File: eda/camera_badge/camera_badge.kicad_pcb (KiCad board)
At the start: 2 copper layers, 111.7 x 76.2 mm, 2 parts, among them U1 ESP32-WROOM-32-DEVKIT

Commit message: badge eda updates
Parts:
- added G***: Silk01, 0_badge:camera_badge_silk01, F.Cu at (97.3, 123.4)
- added G***: Edge, 0_badge:camera_badge_edgecuts, F.Cu at (97.2, 123.3)
- DS1: footprint 0_local:GC9A01_TFT -> 0_local:GC9A01_TFT_Back_Mount
- U1: footprint 0_local:ESP32_DEVKIT_V1 -> 0_local:ESP32_DEVKIT_V1_Back_Mount
- moved U1 96.1 mm to (61.7, 165.2)
- moved DS1 78.5 mm to (84.7, 155.6)
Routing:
- net D23: track 41.0 -> 0.00 mm
- net D18: track 39.6 -> 0.00 mm
- net D16: track 32.6 -> 0.00 mm
- net D4: track 22.1 -> 0.00 mm
- net D5: track 22.0 -> 0.00 mm
- net +3.3V: track 19.9 -> 0.00 mm
- net GND: track 19.9 -> 0.00 mm
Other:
- board size 111.7 x 76.2 mm -> 115 x 204.7 mm

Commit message: eda update
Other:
- board text added: "-- Inside --"
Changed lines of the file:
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@@
     (property "ki_keywords" "GC9A01 TFT Display")
     (attr through_hole)
-    (fp_text reference "DS1" (at -1.5 -2.7) (layer "B.SilkS")
+    (fp_text reference "DS1" (at -1.96 -5.33 180 unlocked) (layer "B.SilkS")
         (effects (font (size 1 1) (thickness 0.15)) (justify mirror))
     )
     (fp_text value "GC9A01 TFT Display" (at 23.25 15.55) (layer "B.Fab")
-        (effects (font (size 1 1) (thickness 0.15)) (justify mirror))
+        (effects (font (size 1 1) (thickness 0.15)))
     )
-    (fp_text user "SCL" (at -2.3 5.15) (layer "B.SilkS")
+    (fp_text user "SCL" (at -2.3 5.15 180 unlocked) (layer "B.SilkS")
         (effects (font (size 0.75 0.75) (thickness 0.15)) (justify mirror))
     )
-    (fp_text user "GND" (at -2.3 2.65) (layer "B.SilkS")
+    (fp_text user "GND" (at -2.3 2.65 180 unlocked) (layer "B.SilkS")
         (effects (font (size 0.75 0.75) (thickness 0.15)) (justify mirror))
     )
-    (fp_text user "CS" (at -2.3 12.78) (layer "B.SilkS")
+    (fp_text user "CS" (at -2.3 12.78 180 unlocked) (layer "B.SilkS")
         (effects (font (size 0.75 0.75) (thickness 0.15)) (justify mirror))
     )
-    (fp_text user "DC" (at -2.3 10.18) (layer "B.SilkS")
+    (fp_text user "DC" (at -2.3 10.18 180 unlocked) (layer "B.SilkS")
         (effects (font (size 0.75 0.75) (thickness 0.15)) (justify mirror))
     )
-    (fp_text user "SDA" (at -2.3 7.72) (layer "B.SilkS")
+    (fp_text user "SDA" (at -2.3 7.72 180 unlocked) (layer "B.SilkS")
         (effects (font (size 0.75 0.75) (thickness 0.15)) (justify mirror))
     )
-    (fp_text user "RST" (at -2.3 15.15) (layer "B.SilkS")
+    (fp_text user "RST" (at -2.3 15.15 180 unlocked) (layer "B.SilkS")
         (effects (font (size 0.75 0.75) (thickness 0.15)) (justify mirror))
     )
-    (fp_text user "VCC" (at -2.3 0.11) (layer "B.SilkS")
+    (fp_text user "VCC" (at -2.3 0.11 180 unlocked) (layer "B.SilkS")
         (effects (font (size 0.75 0.75) (thickness 0.15)) (justify mirror))
     )
@@
     (property "ki_keywords" "RF Radio BT ESP ESP32 Espressif onboard PCB antenna")
     (attr through_hole)
-    (fp_text reference "U1" (at -11.355 -27.36) (layer "B.SilkS")
+    (fp_text reference "U1" (at -11.355 -27.36 180 unlocked) (layer "B.SilkS")
         (effects (font (size 1 1) (thickness 0.15)) (justify mirror))
     )
     (fp_text value "ESP32-WROOM-32-DEVKIT" (at -0.56 27.36) (layer "B.Fab")
-        (effects (font (size 1 1) (thickness 0.15)) (justify mirror))
+        (effects (font (size 1 1) (thickness 0.15)))
     )
-    (fp_text user "ESP32 DEVKIT" (at 0 -15.75 unlocked) (layer "B.SilkS")
+    (fp_text user "ESP32 DEVKIT" (at 0 -15.75 180 unlocked) (layer "B.SilkS")
         (effects (font (size 1 1) (thickness 0.15)) (justify mirror))
     )
-    (fp_text user "USB" (at 0 -22 unlocked) (layer "B.SilkS")
+    (fp_text user "USB" (at 0 -22 180 unlocked) (layer "B.SilkS")
         (effects (font (size 0.75 0.75) (thickness 0.1)) (justify mirror))
     )
@@
     (pad "" np_thru_hole circle (at 23.65 1.25) (size 0.5 0.5) (drill 0.5) (layers "*.Cu" "*.Mask"))
   )
+  (gr_text "-- Inside --" (at 113.8 122) (layer "B.SilkS")
+    (effects (font (size 1 1) (thickness 0.15)) (justify left bottom mirror))
+  )
+  (gr_text "-- Inside --" (at 102.7 125.9 180) (layer "B.SilkS")
+    (effects (font (size 1 1) (thickness 0.15)) (justify left bottom mirror))
+  )
 )

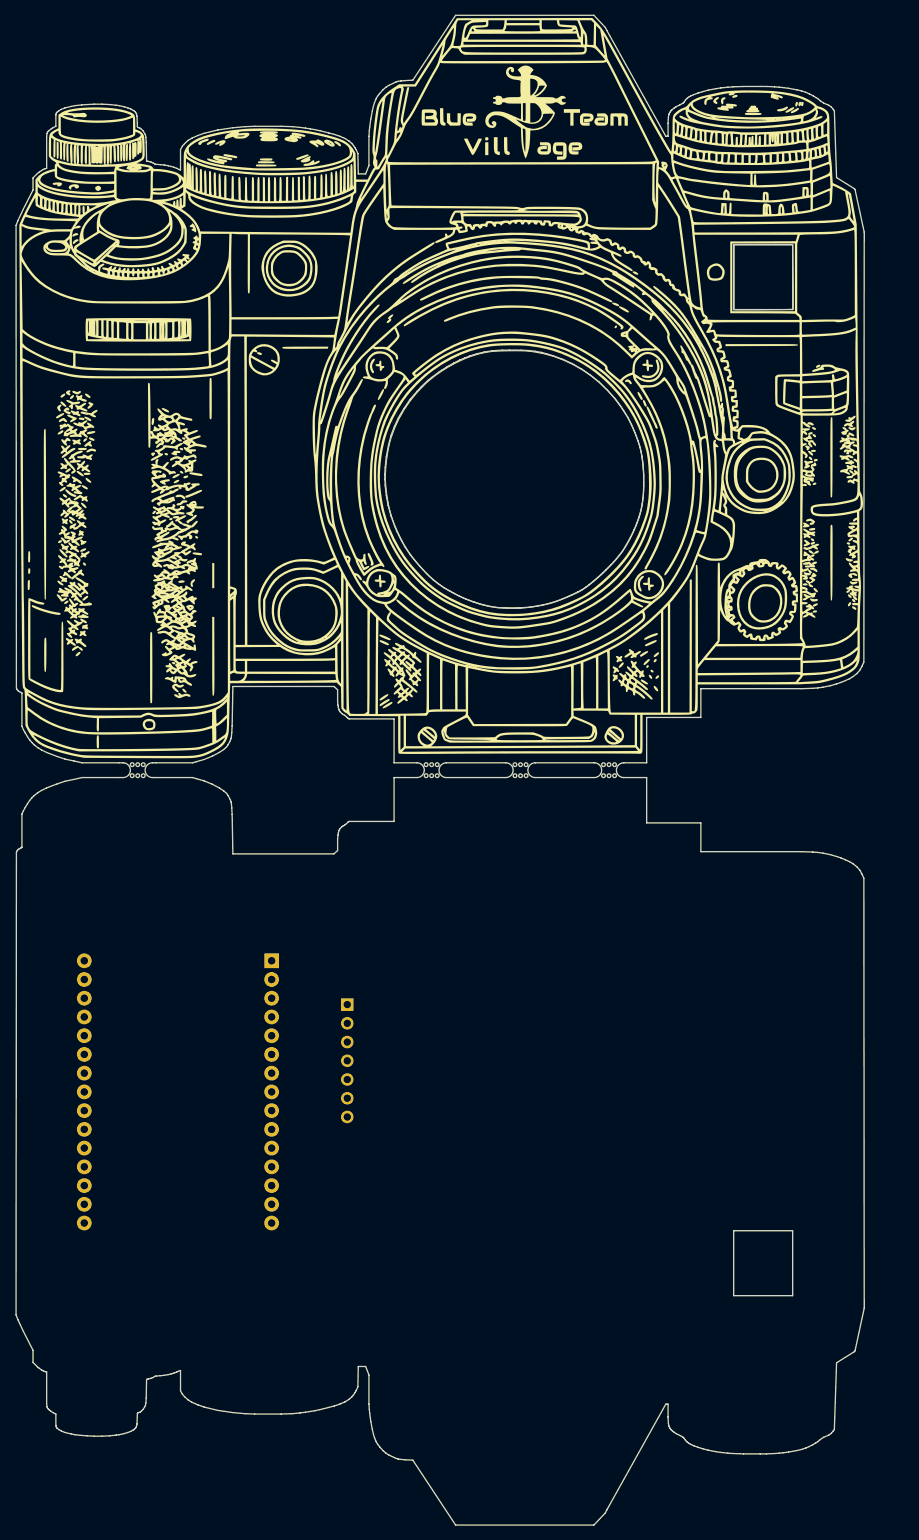
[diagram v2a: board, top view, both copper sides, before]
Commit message: made badge wider
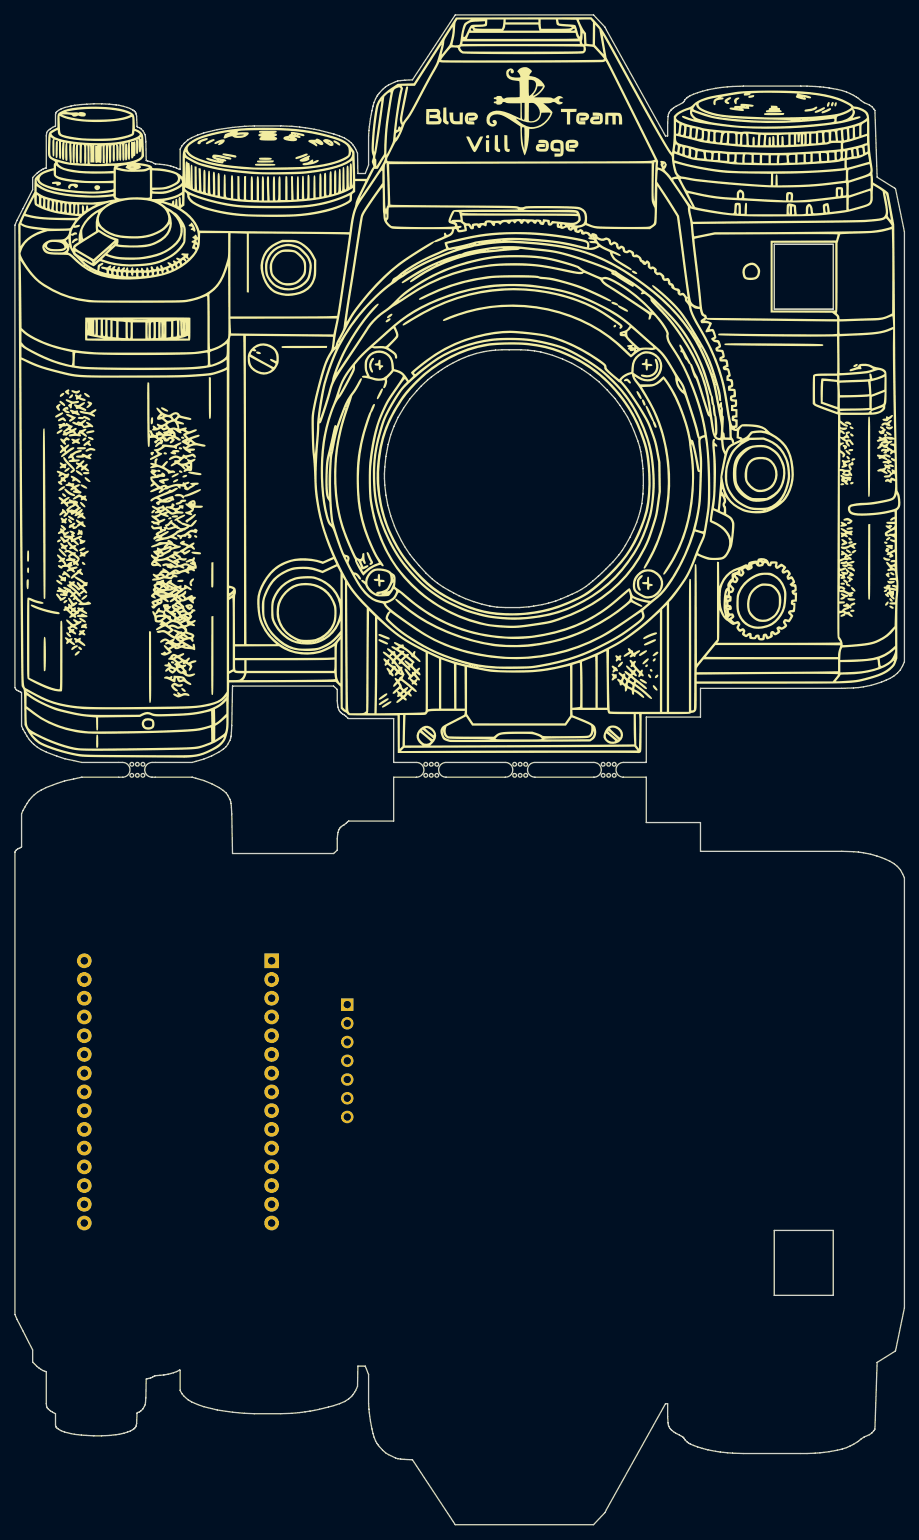
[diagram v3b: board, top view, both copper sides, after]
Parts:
- removed the G*** at (97.3, 123.4)
- added G***: Silk02, 0_badge:camera_badge_silk02, F.Cu at (99.9, 123.8)
- moved G*** 0.07 mm to (97.2, 123.3)
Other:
- board size 115 x 204.7 mm -> 120.6 x 204.7 mm

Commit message: art and fotprint and pcb updates
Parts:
- added badge_bmask01: BMask01, 0_badge:camera_badge_bmask01, F.Cu at (99.9, 123.8)
- added badge_copper01: Copper01, 0_badge:camera_badge_copper01, F.Cu at (99.9, 123.8)
- added badge_fmask01: FMask01, 0_badge:camera_badge_fmask01, F.Cu at (99.9, 123.8)
- renumbered G*** to badge_edgecuts, G*** to badge_silk02

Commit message: footprint and schem updates
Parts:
- removed DS1: GC9A01 TFT Display, 0_local:GC9A01_TFT_Back_Mount
- removed U1: ESP32-WROOM-32-DEVKIT, 0_local:ESP32_DEVKIT_V1_Back_Mount
- added Band_Fastener: Band_Fastener_Hook, 0_local:Band_Fastener_Hook, F.Cu at (140.0, 183.0)
- added Band_Fastener: Band_Fastener_Hook, 0_local:Band_Fastener_Hook, F.Cu at (140.0, 141.0)
- added LIPO: Battery_LIPO_103040_silk_back, 0_local:Battery_LIPO_103040_silk_back, F.Cu at (142.0, 162.0)
- added Lanyard: Lanyard_Hole, 0_local:Lanyard_Hole, F.Cu at (149.3, 208.6)
- added Lanyard: Lanyard_Hole, 0_local:Lanyard_Hole, F.Cu at (50.5, 208.6)

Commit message: pcb work
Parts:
- added BT1: Battery_Lipo, 0_local:Battery_Connector_back, F.Cu at (121.7, 134.2)
- added C10: C_Disc_D3, 0_local:C_Disc_D3_back, F.Cu at (98.2, 203.8)
- added C11: C_Disc_D3, 0_local:C_Disc_D3_back, F.Cu at (121.2, 203.8)
- added C20: C_Disc_D3, 0_local:C_Disc_D3_back, F.Cu at (129.8, 191.8)
- added D10: LED_WS2812D_5mm, 0_local:LED_D5.0mm-4_WS2812D_2024_back, F.Cu at (104.4, 213.2)
- added D11: LED_WS2812D_5mm, 0_local:LED_D5.0mm-4_WS2812D_2024_back, F.Cu at (116.4, 213.2)
- added D2: LED_5mm, 0_local:LED_D5.0mm-2_back, F.Cu at (79.1, 194.1)
- added D20: LED_WS2812D_5mm, 0_local:LED_D5.0mm-4_WS2812D_2024_back, F.Cu at (140.4, 191.0)
- added D3: LED_3mm, 0_local:LED_D3.0mm-2-std_back, F.Cu at (46.3, 130.8)
- added D4: LED_3mm, 0_local:LED_D3.0mm-2-std_back, F.Cu at (44.6, 196.2)
- added D5: LED_3mm, 0_local:LED_D3.0mm-2-std_back, F.Cu at (157.3, 199.9)
- added D6: LED_3mm, 0_local:LED_D3.0mm-2-std_back, F.Cu at (155.5, 138.0)
- added D7: LED_3mm, 0_local:LED_D3.0mm-2-std_back, F.Cu at (109.2, 130.0)
- added DS1: GC9A01 TFT Display, 0_local:GC9A01_TFT_Back_Mount, F.Cu at (114.9, 140.6)
- added J1: Battery_Conn, 0_local:Battery_Connector_back, F.Cu at (59.5, 131.0)
- added J2: Conn_01x05_Socket, 0_local:Conn_Pin_Header_Female_Vert_Back_1x05_Pitch2.54mm, F.Cu at (158.4, 75.0)
- added J3: Conn_01x05_Pin, 0_local:Conn_Pin_Header_Male_Vert_Back_1x05_Pitch2.54mm, F.Cu at (158.4, 172.6)
- added J4: Conn_01x05_Socket, 0_local:Conn_Pin_Header_Female_Vert_Back_1x05_Pitch2.54mm, F.Cu at (113.6, 44.5)
- added J5: Conn_01x05_Pin, 0_local:Conn_Pin_Header_Male_Vert_Back_1x05_Pitch2.54mm, F.Cu at (113.6, 203.1)
- added J6: Conn_01x05_Socket, 0_local:Conn_Pin_Header_Female_Vert_Back_1x05_Pitch2.54mm, F.Cu at (146.0, 109.6)
- added J7: Conn_01x05_Pin, 0_local:Conn_Pin_Header_Male_Vert_Back_1x05_Pitch2.54mm, F.Cu at (146.0, 138.0)
- added J8: Conn_01x05_Socket, 0_local:Conn_Pin_Header_Female_Vert_Back_1x05_Pitch2.54mm, F.Cu at (42.0, 75.0)
- added J9: Conn_01x05_Pin, 0_local:Conn_Pin_Header_Male_Vert_Back_1x05_Pitch2.54mm, F.Cu at (42.0, 172.6)
- added JSAO1: Conn_02x03_SAO, 0_sao_v169bis:SAOv169-BADGEv2-2x3_gpio_back, F.Cu at (108.6, 24.9)
- added R10: 47R_6.3mm, 0_local:R_Axial_DIN0207_L6.3_D2.5_P7.62_Horiz_back, F.Cu at (91.0, 198.1)
- added R2: 47R_6.3mm, 0_local:R_Axial_DIN0207_L6.3_D2.5_P7.62_Horiz_back, F.Cu at (84.2, 198.1)
- added R20: 47R_6.3mm, 0_local:R_Axial_DIN0207_L6.3_D2.5_P7.62_Horiz_back, F.Cu at (131.6, 187.2)
- added R3: 47R_6.3mm, 0_local:R_Axial_DIN0207_L6.3_D2.5_P7.62_Horiz_back, F.Cu at (46.6, 137.4)
- added R4: 47R_6.3mm, 0_local:R_Axial_DIN0207_L6.3_D2.5_P7.62_Horiz_back, F.Cu at (42.6, 188.7)
- added R5: 47R_6.3mm, 0_local:R_Axial_DIN0207_L6.3_D2.5_P7.62_Horiz_back, F.Cu at (157.3, 193.9)
- added R6: 47R_6.3mm, 0_local:R_Axial_DIN0207_L6.3_D2.5_P7.62_Horiz_back, F.Cu at (158.3, 143.7)
- added R7: 47R_6.3mm, 0_local:R_Axial_DIN0207_L6.3_D2.5_P7.62_Horiz_back, F.Cu at (112.4, 130.0)
- added SW1: SW_SPDT_SS12D00G, 0_local:SW_SPDT_Slide_SS12D00G-1P2T_3pin_back, F.Cu at (97.3, 128.7)
- added U1: ESP32-WEMOS-LOLIN32-LITE, 0_local:ESP32_WEMOS_LOLIN32_LITE_back, F.Cu at (69.0, 163.2)
- moved Band_Fastener 8.14 mm to (132.0, 181.5)
- moved Band_Fastener 8.14 mm to (132.0, 139.5)
- moved LIPO 1.55 mm to (141.6, 160.5)

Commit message: pcb updates
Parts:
- moved R10 13.8 mm to (104.8, 196.8), turned to 0 degrees
- moved R20 11.2 mm to (120.4, 187.0)
- moved R4 7.29 mm to (46.3, 195.0)
- moved D4 4.17 mm to (46.3, 200.0)
- moved C20 3.51 mm to (133.2, 192.0), turned to 90 degrees
- moved D20 2.52 mm to (138.8, 192.9), turned to 90 degrees
- moved R3 2.41 mm to (46.3, 135.0)
- moved R5 2.11 mm to (155.5, 195.0)
- moved D5 1.78 mm to (155.5, 200.0)
- moved SW1 1.55 mm to (98.2, 130.0)
- moved J1 1.00 mm to (59.5, 130.0)
- moved D3 0.80 mm to (46.3, 130.0)
- moved R7 0.69 mm to (113.1, 130.0)
- moved C10 0.62 mm to (98.2, 203.1)
- moved C11 0.62 mm to (121.2, 203.1)
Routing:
- net +3.3V: track 0.00 -> 191.5 mm
- net 0: track 0.00 -> 102.4 mm
- net 12: track 0.00 -> 87.2 mm
- net 15: track 0.00 -> 76.1 mm
- net 17: track 0.00 -> 69.9 mm
- net 2: track 0.00 -> 59.9 mm
- net 14: track 0.00 -> 52.5 mm
- net 19: track 0.00 -> 49.5 mm
- net 26: track 0.00 -> 48.3 mm
- net VBAT: track 0.00 -> 47.9 mm
- net 23: track 0.00 -> 45.1 mm
- net 18: track 0.00 -> 44.2 mm
- net 5: track 0.00 -> 38.9 mm
- net 27: track 0.00 -> 37.7 mm
- net 16: track 0.00 -> 34.3 mm
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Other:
- board text added: "ON - OFF"
